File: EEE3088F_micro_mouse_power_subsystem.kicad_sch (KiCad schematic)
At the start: 2 parts, among them J1 Conn_02x16_Odd_Even, J2 Conn_01x02

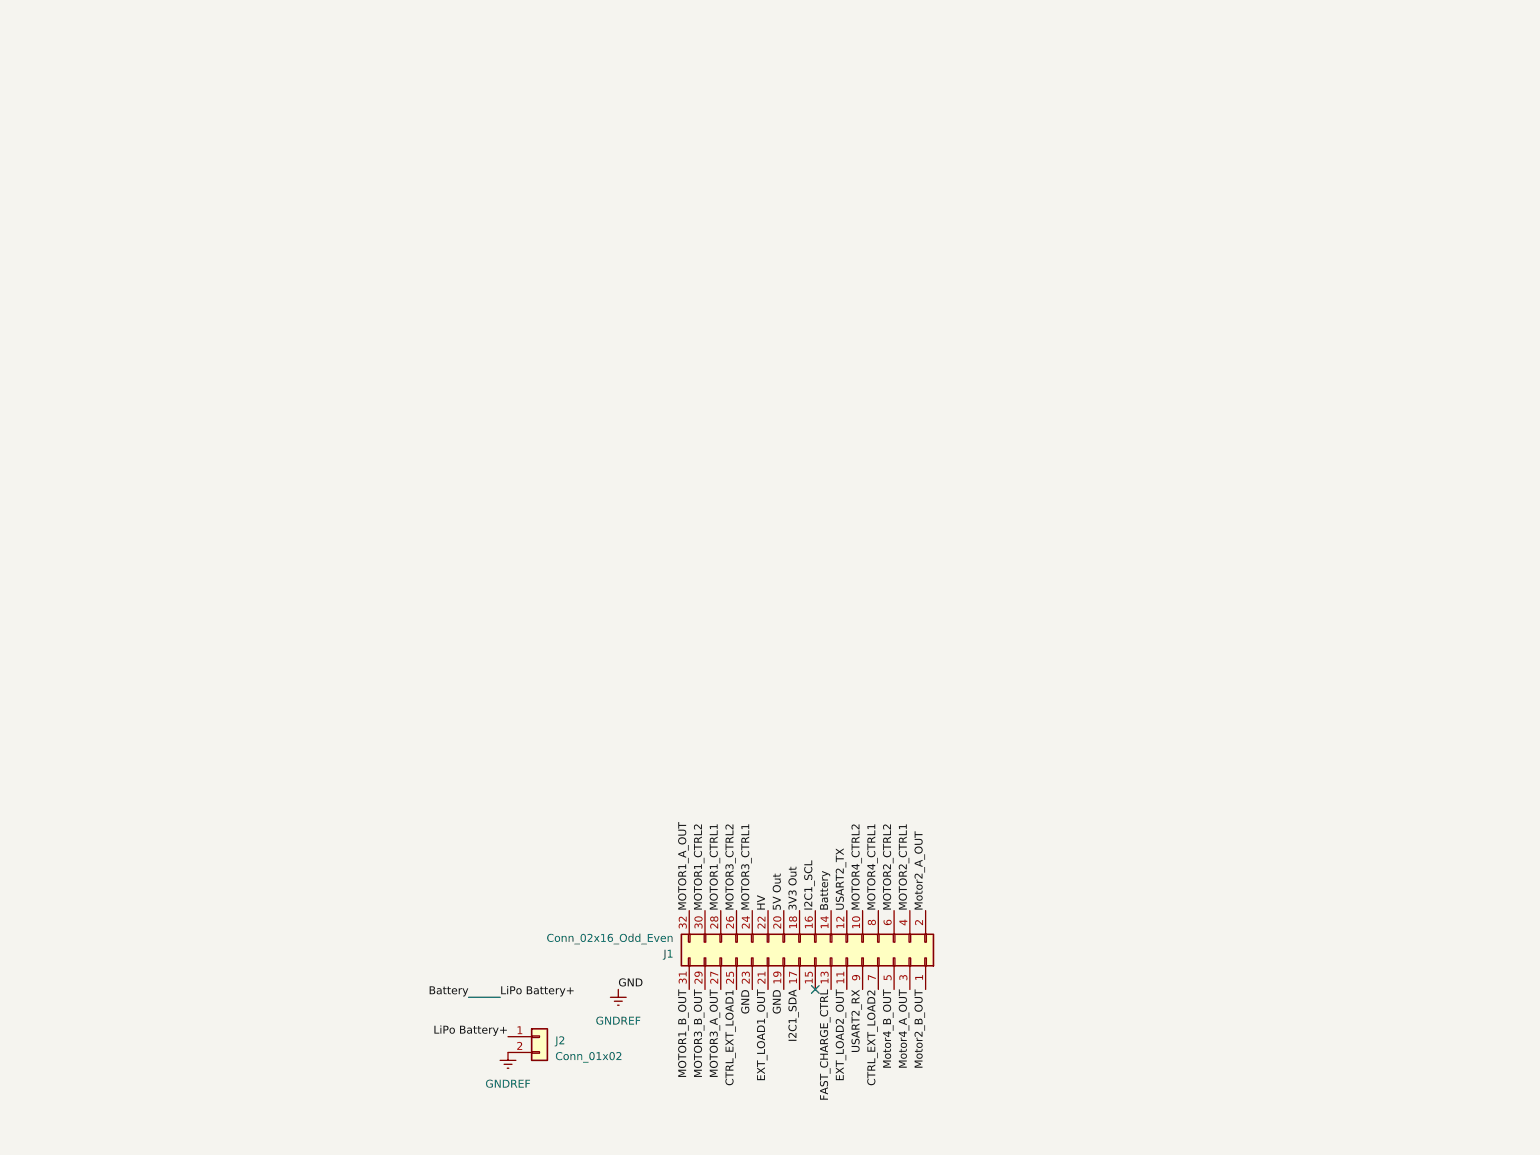
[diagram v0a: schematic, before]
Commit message: Added circuit for Requirement 2
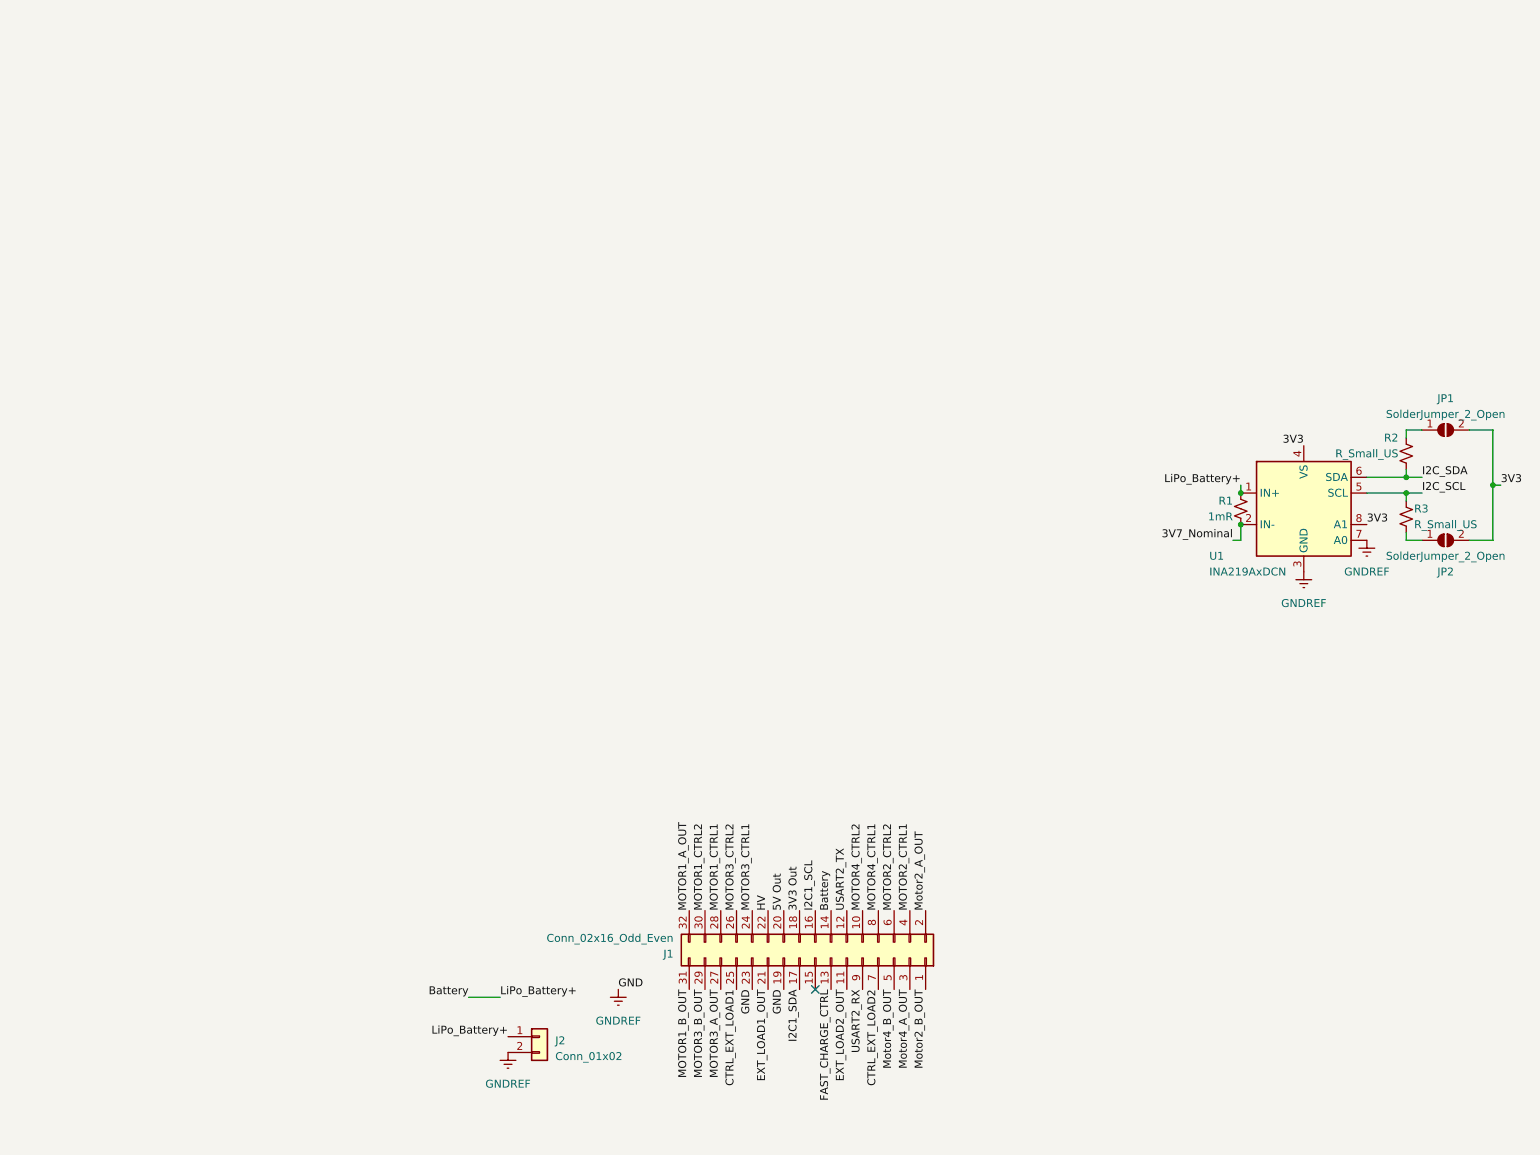
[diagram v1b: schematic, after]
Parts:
- added JP1, JP2: SolderJumper_2_Open, symbol Jumper:SolderJumper_2_Open
- added R1: 1mR, symbol Device:R_Small_US
- added R2, R3: R_Small_US, symbol Device:R_Small_US
- added U1: INA219AxDCN, Package_TO_SOT_SMD:SOT-23-8, symbol Sensor_Energy:INA219AxDCN
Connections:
- net Battery: now also R1.1, U1.1 (IN+)
- net GNDREF: now also U1.3 (GND), U1.7 (A0)
- new net: JP2.1 (A), R3.2
- new net: JP1.1 (A), R2.1
- new net 3V3: JP1.2 (B), JP2.2 (B), U1.4 (VS), U1.8 (A1)
- new net 3V7_Nominal: R1.2, U1.2 (IN-)
- new net I2C_SCL: R3.1, U1.5 (SCL)
- new net I2C_SDA: R2.2, U1.6 (SDA)

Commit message: Added circuit for Requirement 1
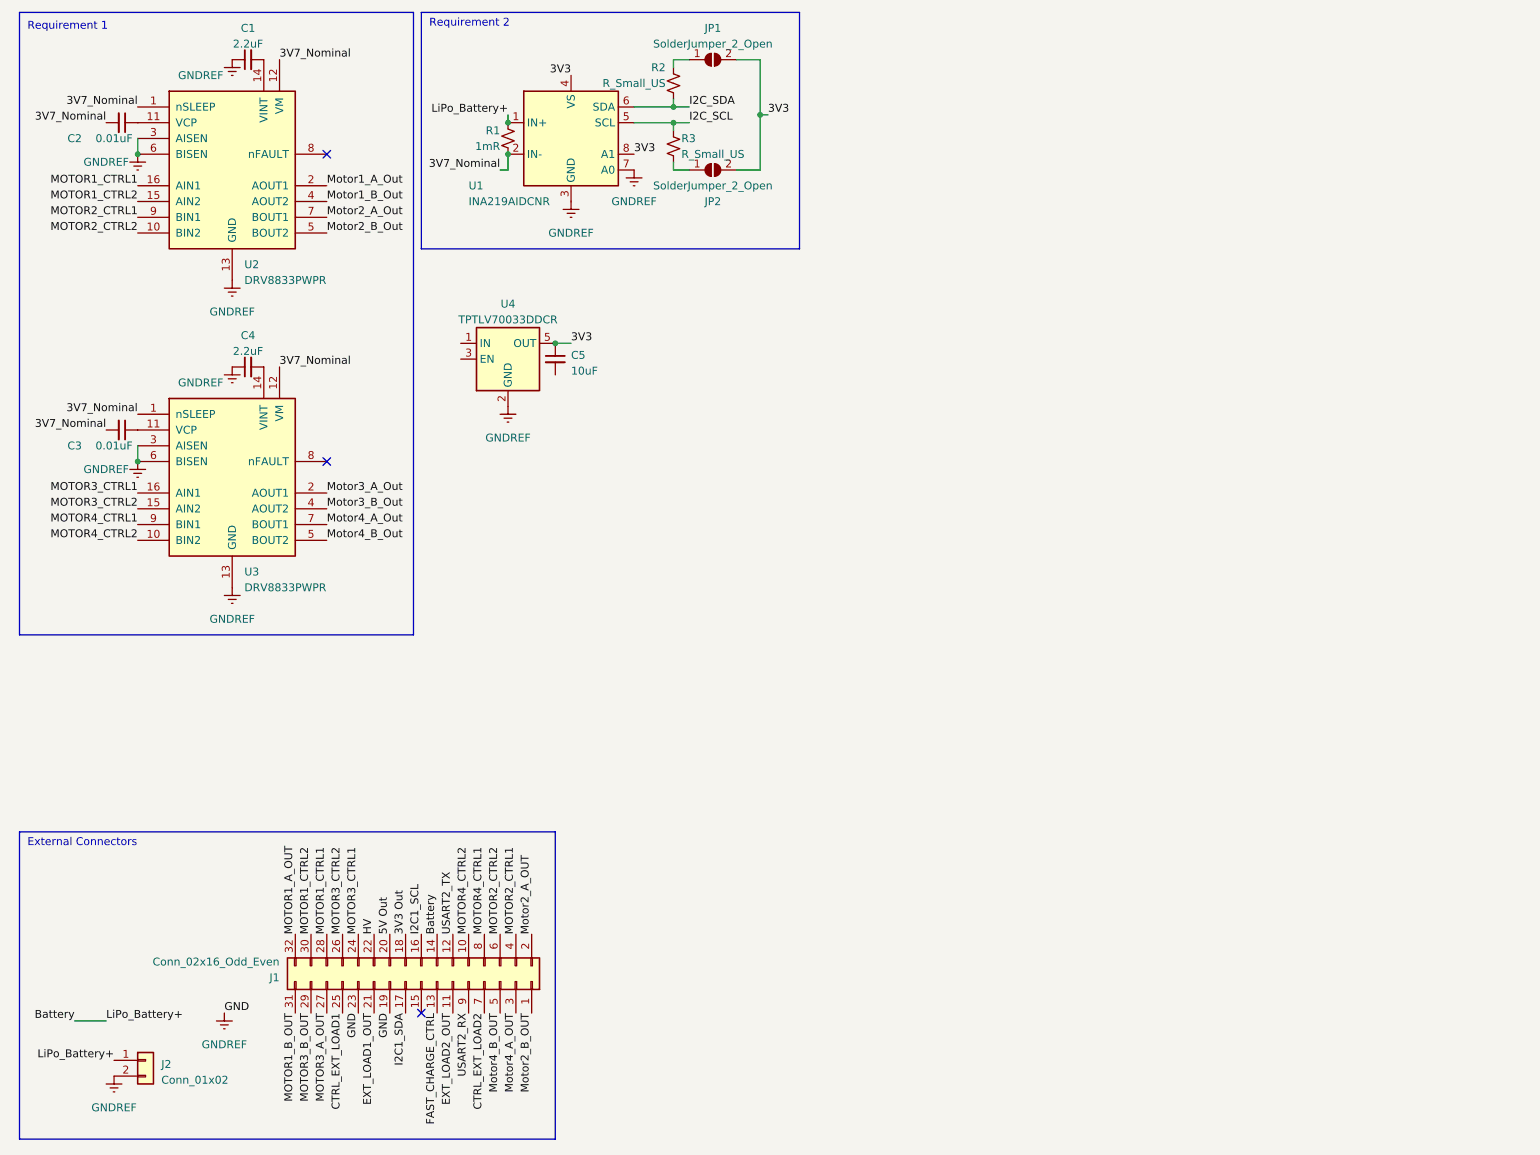
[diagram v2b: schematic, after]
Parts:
- added C1, C4: 2.2uF, symbol Device:C_Small
- added C2, C3: 0.01uF, symbol Device:C_Small
- added C5: 10uF, symbol Device:C_Small
- added U2, U3: DRV8833PWPR, Package_SO:TSSOP-16_4.4x5mm_P0.65mm, symbol Driver_Motor:DRV8833PW
- added U4: TPTLV70033DDCR, Package_TO_SOT_SMD:SOT-23-5, symbol Regulator_Linear:TPS78233DDC
- U1: value INA219AxDCN -> INA219AIDCNR
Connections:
- net 3V3: now also C5.1, U4.5 (OUT)
- net 3V7_Nominal: now also C2.2, C3.2, U2.1 (nSLEEP), U2.12 (VM), U3.1 (nSLEEP), U3.12 (VM)
- net GNDREF: now also C1.1, C4.1, U2.13 (GND), U2.3 (AISEN), U2.6 (BISEN), U3.13 (GND), U3.3 (AISEN), U3.6 (BISEN), U4.2 (GND), U4.4 (GND)
- net MOTOR1_CTRL1: now also U2.16 (AIN1)
- net MOTOR1_CTRL2: now also U2.15 (AIN2)
- net MOTOR2_CTRL1: now also U2.9 (BIN1)
- net MOTOR2_CTRL2: now also U2.10 (BIN2)
- net MOTOR3_CTRL1: now also U3.16 (AIN1)
- net MOTOR3_CTRL2: now also U3.15 (AIN2)
- net MOTOR4_CTRL1: now also U3.9 (BIN1)
- net MOTOR4_CTRL2: now also U3.10 (BIN2)
- new net: C4.2, U3.14 (VINT)
- new net: C1.2, U2.14 (VINT)
- new net: C2.1, U2.11 (VCP)
- new net: C3.1, U3.11 (VCP)
- new net Motor1_A_Out: U2.2 (AOUT1)
- new net Motor1_B_Out: U2.4 (AOUT2)
- new net Motor2_A_Out: U2.7 (BOUT1)
- new net Motor2_B_Out: U2.5 (BOUT2)
- new net Motor3_A_Out: U3.2 (AOUT1)
- new net Motor3_B_Out: U3.4 (AOUT2)
- new net Motor4_A_Out: U3.7 (BOUT1)
- new net Motor4_B_Out: U3.5 (BOUT2)
- no-connect marks 1 -> 3
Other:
- note added: "External Connectors"
- note added: "Requirement 1"
- note added: "Requirement 2"
- moved on the sheet: J1, J2, JP1, JP2, R1, R2, R3, U1

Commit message: test commit
Just testing
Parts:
- added C6: C, symbol Device:C

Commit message: Updated LCSC numbers and Requirements 7 and 8
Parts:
- removed C6: C, symbol Device:C
- added C6: 22uF, symbol Device:C_Small
- added D1: CRS08, symbol Device:D_Small
- added L1: 4.7uH, symbol Device:L_Small
- added R4: 27kR, symbol Device:R_Small_US
- added R5: 220kR, symbol Device:R_Small_US
- added R6: 18kR, symbol Device:R_Small_US
- added R7: 12kR, symbol Device:R_Small_US
- added U5: MT3608L, Package_TO_SOT_SMD:SOT-23-6, symbol Regulator_Switching:AP3211K
- C1, C4: LCSC (none) -> C12530
- C2, C3: LCSC (none) -> C15195
- C5: LCSC (none) -> C15525
- R1: LSCS (none) -> C7419993
- U1: LCSC (none) -> C87469
- U2: LCSC (none) -> C50506
- U3: LSCS (none) -> C50506
- U4: LCSC (none) -> C2937039
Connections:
- net GNDREF: now also R4.2, R7.2, U5.2 (GND)
- new net: R5.2, R6.1, U5.3 (FB)
- new net: R6.2, R7.1
- new net: D1.2 (A), L1.2, U5.1 (SW)
- new net: L1.1, U5.4 (EN), U5.5 (VIN)
- new net: R4.1, U5.6 (OC)
- new net 5V: C6.1, D1.1 (K), R5.1
